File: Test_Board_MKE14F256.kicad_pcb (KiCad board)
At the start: 4 copper layers, 115 parts, among them P1 CONN_01X02, P10 CONN_01X01, P11 CONN_01X01, P12 CONN_01X01, P13 CONN_01X01, P14 CONN_01X01, P15 CONN_01X01, P16 CONN_01X01, P17 CONN_01X01, P18 CONN_01X01, P19 CONN_01X01, P2 CONN_01X04, P20 CONN_01X01, P21 CONN_01X01, P22 CONN_01X01, P23 CONN_01X01, P24 CONN_01X01, P25 CONN_01X01, P26 CONN_01X01, P27 CONN_01X01, P28 CONN_01X04, P5 CONN_01X05, P6 CONN_01X04, P7 CONN_01X01, P8 CONN_01X01, P9 CONN_01X01, U1 TS30042, U2 NCP700B, U3 MIC2288, U4 ADS79XX, U5 REF3030, U6 TSV524A, U7 MKE14F256_v.1.2, Y1 ABMM2-8.000MHZ-E2-T

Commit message: changed usd slot
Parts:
- XS1: footprint .pretty:uSDcard -> .pretty:HIROSE-MICROSD-DM3AT-SF
- moved R27 153.8 mm to (26.7, 31.0)
- moved R26 150.1 mm to (26.7, 38.7)
- moved D7 149.3 mm to (33.3, 31.6)
- moved D8 144.1 mm to (34.4, 40.1)
- moved R25 143.0 mm to (268.8, 17.0)
- moved C29 139.2 mm to (266.2, 19.3)
- moved C33 138.5 mm to (42.5, 35.3)
- moved C35 134.8 mm to (43.6, 40.5)
- moved XS1 126.4 mm to (267.4, 38.5)
- moved R22 117.0 mm to (265.9, 157.4)
- moved R21 116.2 mm to (266.8, 153.0)
- moved R20 115.2 mm to (267.9, 147.4)
- moved R19 113.9 mm to (268.3, 142.0)
- moved D6 112.5 mm to (261.2, 156.7)
- moved P28 110.9 mm to (29.8, 101.9)
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
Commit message: All parts in places (exept :Leds)
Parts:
- moved R27 160.3 mm to (181.8, 71.3)
- moved R26 159.2 mm to (181.8, 74.8)
- moved P6 158.0 mm to (188.2, 67.0), turned to 270 degrees
- moved P2 151.0 mm to (188.2, 61.8), turned to 90 degrees
- moved D7 148.5 mm to (176.4, 71.3), turned to 180 degrees
- moved D8 146.2 mm to (176.4, 74.8), turned to 180 degrees
- moved C33 142.1 mm to (179.0, 74.8), turned to 270 degrees
- moved C35 138.8 mm to (179.0, 71.3), turned to 270 degrees
- moved P28 118.4 mm to (146.3, 80.6), turned to 90 degrees
- moved C1 115.9 mm to (158.3, 92.1)
- moved C38 115.9 mm to (159.2, 89.8)
- moved L1 115.9 mm to (164.3, 83.0)
- moved C3 115.9 mm to (161.3, 83.1)
- moved U1 115.9 mm to (163.3, 88.5)
- moved C4 115.9 mm to (158.9, 83.1)
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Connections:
- P2 pad 1: V_in_4 -> V_in_3
- P2 pad 3: V_in_3 -> V_in_2
- P2 pad 5: V_in_2 -> V_in_4
- R31 pad 2: Net-(R31-Pad2) -> OpAmp_Out2
- R32 pad 2: Net-(R32-Pad2) -> OpAmp_Out4
- R5 pad 1: ADC_2 -> OpAmp_Out2
- R6 pad 1: ADC_1 -> OpAmp_Out4
- U6 pad 13: Net-(R32-Pad2) -> OpAmp_Out4
- U6 pad 14: Net-(R32-Pad2) -> OpAmp_Out4
- U6 pad 8: Net-(R31-Pad2) -> OpAmp_Out2
- U6 pad 9: Net-(R31-Pad2) -> OpAmp_Out2
- U7 pad 51: ADC_1 -> ADC_3
- U7 pad 52: ADC_2 -> ADC_1
- U7 pad 53: ADC_3 -> ADC_4
- U7 pad 54: ADC_4 -> ADC_2
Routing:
- net V_in_4: track 0.00 -> 34.5 mm
- net V_in_2: track 0.00 -> 30.6 mm
- net ADC_3: track 0.00 -> 16.5 mm
- net ADC_2: track 0.00 -> 15.1 mm
- net V_in_3: track 0.00 -> 14.9 mm
- net +3V3: track 0.00 -> 7.65 mm, vias 0 -> 2
- net ADC_1: track 0.00 -> 7.49 mm
- net ADC_4: track 0.00 -> 5.40 mm
- net GND: track 0.00 -> 5.06 mm
- net Net-(C23-Pad1): track 0.00 -> 4.65 mm
- net Net-(C19-Pad1): track 0.00 -> 4.60 mm
- net Net-(C18-Pad1): track 0.00 -> 4.55 mm
- net Net-(C24-Pad1): track 0.00 -> 4.53 mm
- net Net-(R30-Pad2): track 0.00 -> 2.60 mm
- net OpAmp_Out2: track 0.00 -> 2.58 mm
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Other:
- net class Default: via_dia 0.6 -> 0.65; via_drill 0.4 -> 0.3

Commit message: Started with tracking
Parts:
- moved P22 61.3 mm to (65.1, 118.8)
- moved P23 61.3 mm to (65.1, 118.8)
- moved P24 61.3 mm to (65.1, 118.8)
- moved P25 61.3 mm to (65.1, 118.8)
- moved P26 61.3 mm to (65.1, 118.8)
- moved P27 61.3 mm to (65.1, 118.8)
- moved LS 35.4 mm to (93.8, 124.8)
- moved HS 32.5 mm to (94.3, 117.7)
- moved DC_Vin 23.7 mm to (102.1, 109.9)
- moved GND 22.6 mm to (112.9, 128.2)
- moved ADC_4 20.1 mm to (145.8, 109.7)
- moved GND 18.9 mm to (112.7, 123.2)
- moved ADC_3 18.7 mm to (143.2, 116.1)
- moved Vref 18.5 mm to (134.4, 125.8)
- moved GND 17.2 mm to (122.4, 126.3)
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- renumbered P11 to +3.3V, P16 to +3.3V, P7 to ADC_1, P8 to ADC_2, P9 to ADC_3, P10 to ADC_4, P17 to DC_3V6, P18 to DC_Vin, P12 to GND, P13 to GND, P14 to GND, P15 to GND, P20 to HS, P21 to LS, P19 to Vref
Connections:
- Y1 pad 2: Net-(C28-Pad1) -> (no net)
- Y1 pad 3: (no net) -> Net-(C28-Pad1)
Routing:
- net GND: track 5.06 -> 47.3 mm, vias 0 -> 14
- net +3V3: track 7.65 -> 45.0 mm, vias 2 -> 8
- net uSD_SPI0_CS0: track 0.00 -> 16.6 mm
- net uSD_SPI0_DI: track 0.00 -> 15.3 mm
- net uSD_SPI0_SCLK: track 0.00 -> 15.2 mm
- net UART1_RX: track 0.00 -> 14.0 mm
- net uSD_SPI0_DO: track 0.00 -> 13.7 mm
- net Net-(C28-Pad1): track 0.00 -> 11.6 mm
- net UART1_TX: track 0.00 -> 11.3 mm
- net Net-(C27-Pad1): track 0.00 -> 11.1 mm
- net Net-(P6-Pad2): track 0.00 -> 5.16 mm
- net Net-(P6-Pad3): track 0.00 -> 4.71 mm
- net (no net): track 0.00 -> 4.46 mm, vias 0 -> 1
- net Vref: track 0.00 -> 3.43 mm
- net ADC_3: track 16.5 -> 19.4 mm
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
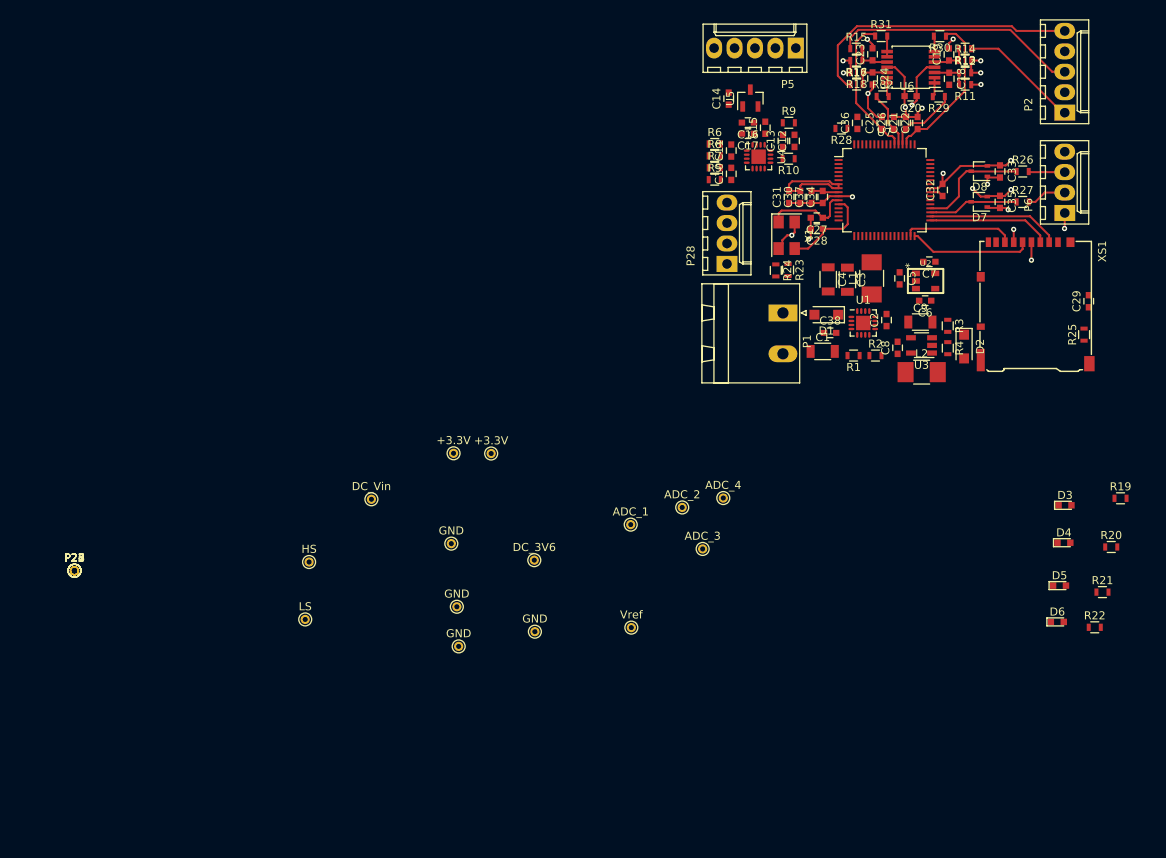
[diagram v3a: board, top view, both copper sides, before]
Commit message: added missing parts (SPI conn / Boost Conn/ drills..)
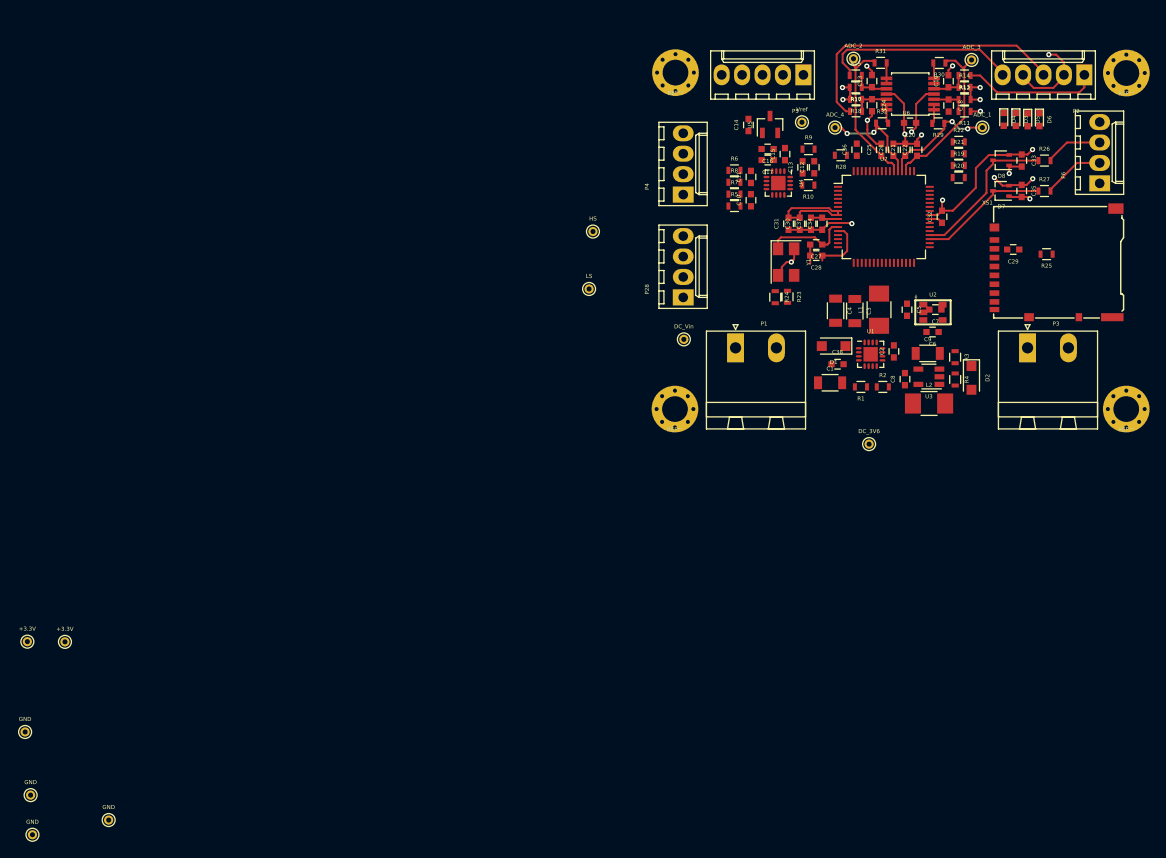
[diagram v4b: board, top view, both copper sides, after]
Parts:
- removed P22, P23, P24, P25, P26, P27: CONN_01X01, Connect:PINTST
- added P3: CONN_01X02, Connectors_Phoenix:PhoenixContact_MSTBA-G_02x5.08mm_Angled, F.Cu at (183.6, 91.1)
- added P4: CONN_01X04, Connectors_Molex:Molex_KK-6410-04_04x2.54mm_Straight, F.Cu at (140.8, 72.0)
- added REF**: 3mm_holes, .pretty:3mm_holes, F.Cu at (139.8, 98.7)
- added REF**: 3mm_holes, .pretty:3mm_holes, F.Cu at (139.9, 56.8)
- added REF**: 3mm_holes, .pretty:3mm_holes, F.Cu at (195.9, 98.7)
- added REF**: 3mm_holes, .pretty:3mm_holes, F.Cu at (195.9, 56.9)
- moved ADC_3 69.4 mm to (176.7, 55.3)
- moved Vref 66.3 mm to (155.6, 63.0)
- moved ADC_1 65.9 mm to (178.0, 63.7)
- moved R22 62.7 mm to (175.1, 65.5)
- moved D6 62.5 mm to (185.1, 62.7), turned to 270 degrees
- moved ADC_2 59.7 mm to (162.0, 55.1)
- moved D5 58.0 mm to (183.6, 62.7), turned to 270 degrees
- moved GND 57.9 mm to (59.7, 146.7)
- moved GND 57.9 mm to (59.9, 151.6)
- moved +3.3V 57.9 mm to (59.3, 127.6)
- moved GND 57.9 mm to (59.0, 138.8)
- moved GND 57.9 mm to (69.4, 149.8)
- moved +3.3V 57.9 mm to (64.0, 127.6)
- moved R21 57.3 mm to (175.1, 66.9)
- moved HS 54.2 mm to (129.6, 76.6)
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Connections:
- P2 pad 3: V_in_2 -> V_in_4
- P2 pad 5: V_in_4 -> V_in_2
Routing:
- net uSD_SPI0_CS0: track 16.6 -> 0.29 mm
- net uSD_SPI0_DI: track 15.3 -> 0.00 mm
- net uSD_SPI0_SCLK: track 15.2 -> 0.00 mm
- net uSD_SPI0_DO: track 13.7 -> 0.00 mm
- net GND: track 47.3 -> 55.9 mm, vias 14 -> 13
- net ADC_4: track 7.08 -> 13.5 mm, vias 0 -> 2
- net V_in_2: track 30.6 -> 24.6 mm
- net UART1_RX: track 14.0 -> 19.3 mm
- net ADC_1: track 9.03 -> 14.3 mm, vias 0 -> 2
- net UART1_TX: track 11.3 -> 16.3 mm
- net Net-(C28-Pad1): track 11.6 -> 7.35 mm
- net Net-(P6-Pad3): track 4.71 -> 7.39 mm
- net Net-(P6-Pad2): track 5.16 -> 7.68 mm
- net +3V3: track 45.0 -> 46.9 mm, vias 8 -> 6
- net V_in_3: track 14.9 -> 16.8 mm
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
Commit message: still the regulators & Planes fill
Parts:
- added P10, P11, P12, P13, P14, P15, P16, P17, P18, P19, P20, P21, P22, P23, P24, P25, P26, P27, P7, P8, P9: CONN_01X01, Connect:PINTST, F.Cu at (168.1, 112.3)
- moved +3.3V 41.2 mm to (93.4, 104.4)
- moved GND 41.2 mm to (103.5, 126.5)
- moved GND 41.2 mm to (93.1, 115.6)
- moved +3.3V 41.2 mm to (98.0, 104.4)
- moved GND 41.2 mm to (93.8, 123.4)
- moved GND 41.2 mm to (94.0, 128.4)
- moved Vref 16.5 mm to (147.8, 77.7)
- moved C14 12.4 mm to (150.5, 75.7)
- moved U5 12.2 mm to (153.1, 75.5)
- moved R25 9.80 mm to (176.2, 79.9), turned to 90 degrees
- moved C4 5.60 mm to (165.3, 85.7), turned to 180 degrees
- moved C29 5.29 mm to (177.7, 82.1), turned to 90 degrees
- moved R22 5.15 mm to (174.9, 70.6)
- moved L1 4.56 mm to (165.2, 90.9), turned to 0 degrees
- moved C31 4.40 mm to (156.9, 72.4), turned to 0 degrees
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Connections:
- U1 pad 16: Net-(U1-Pad16) -> Net-(C2-Pad2)
- U7 pad 25: led_red -> Net-(U7-Pad25)
- U7 pad 26: led_yel -> ADC_PDEN
- U7 pad 27: led_grn -> Net-(U7-Pad27)
- U7 pad 28: led_blu -> Net-(U7-Pad28)
- U7 pad 43: ADC_PDEN -> Net-(U7-Pad43)
- U7 pad 47: Net-(U7-Pad47) -> led_blu
- U7 pad 48: Net-(U7-Pad48) -> led_red
- U7 pad 49: Net-(U7-Pad49) -> led_grn
- U7 pad 50: Net-(U7-Pad50) -> led_yel
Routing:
- net GND: track 55.9 -> 122.1 mm, vias 13 -> 28
- net ADC_SPI1_MOSI_ADC_CH_SEL: track 0.00 -> 51.0 mm, vias 0 -> 2
- net ADC_SPI1_CS0: track 0.00 -> 45.6 mm, vias 0 -> 2
- net OpAmp_Out2: track 2.58 -> 39.3 mm, vias 0 -> 2
- net ADC_SPI1_SCLK: track 0.00 -> 31.6 mm, vias 0 -> 1
- net Vref: track 3.43 -> 33.6 mm, vias 0 -> 4
- net ADC_SPI1_SDO: track 0.00 -> 28.3 mm, vias 0 -> 1
- net OpAmp_Out4: track 2.41 -> 27.3 mm, vias 0 -> 2
- net SWD_RESET: track 0.00 -> 21.0 mm
- net ADC_PDEN: track 0.00 -> 19.1 mm, vias 0 -> 2
- net SWD_DIO_TGTMCU: track 0.00 -> 18.5 mm, vias 0 -> 1
- net SWD_CLK: track 0.00 -> 17.0 mm, vias 0 -> 2
- net Net-(D6-Pad2): track 0.00 -> 16.2 mm
- net Net-(C12-Pad1): track 0.00 -> 15.9 mm
- net DC_Vin: track 0.00 -> 14.8 mm
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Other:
- board outline added: 62.8 x 49.7 mm

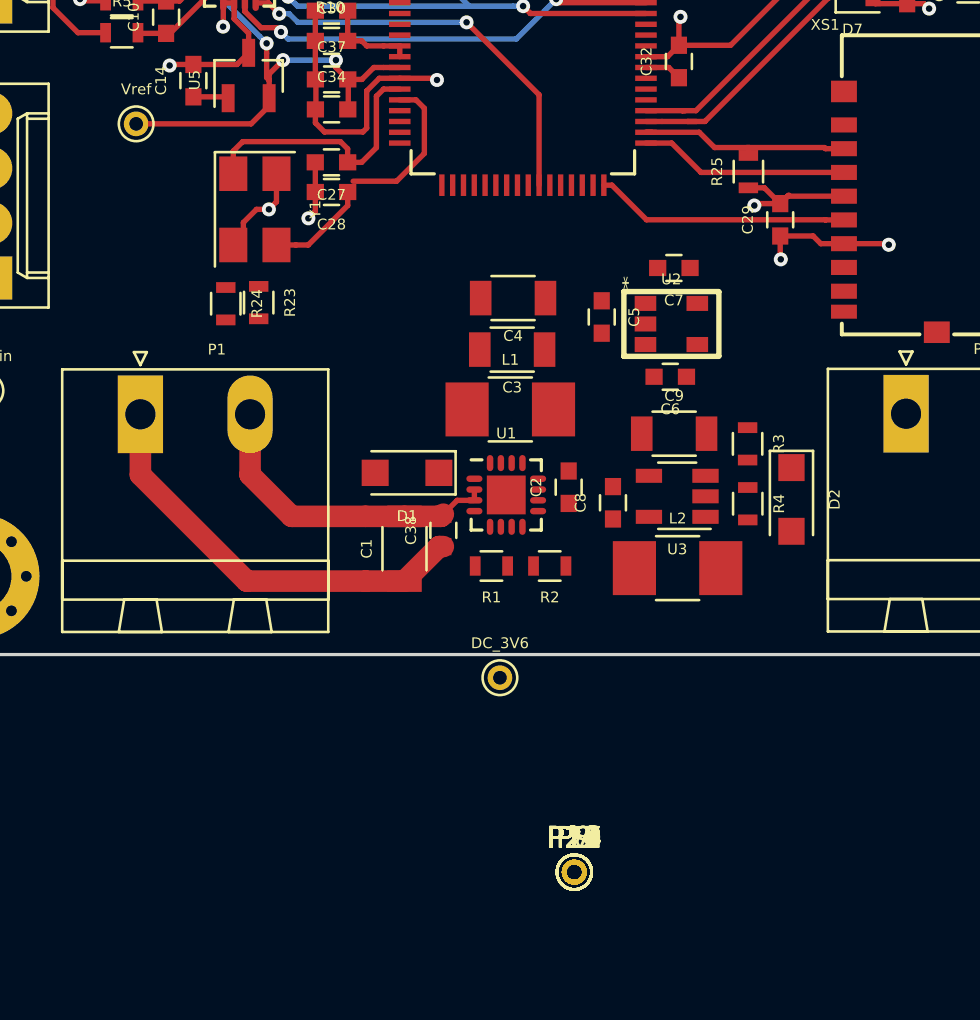
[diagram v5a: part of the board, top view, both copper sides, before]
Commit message: routed the Buck & LDO ==> Still Boost
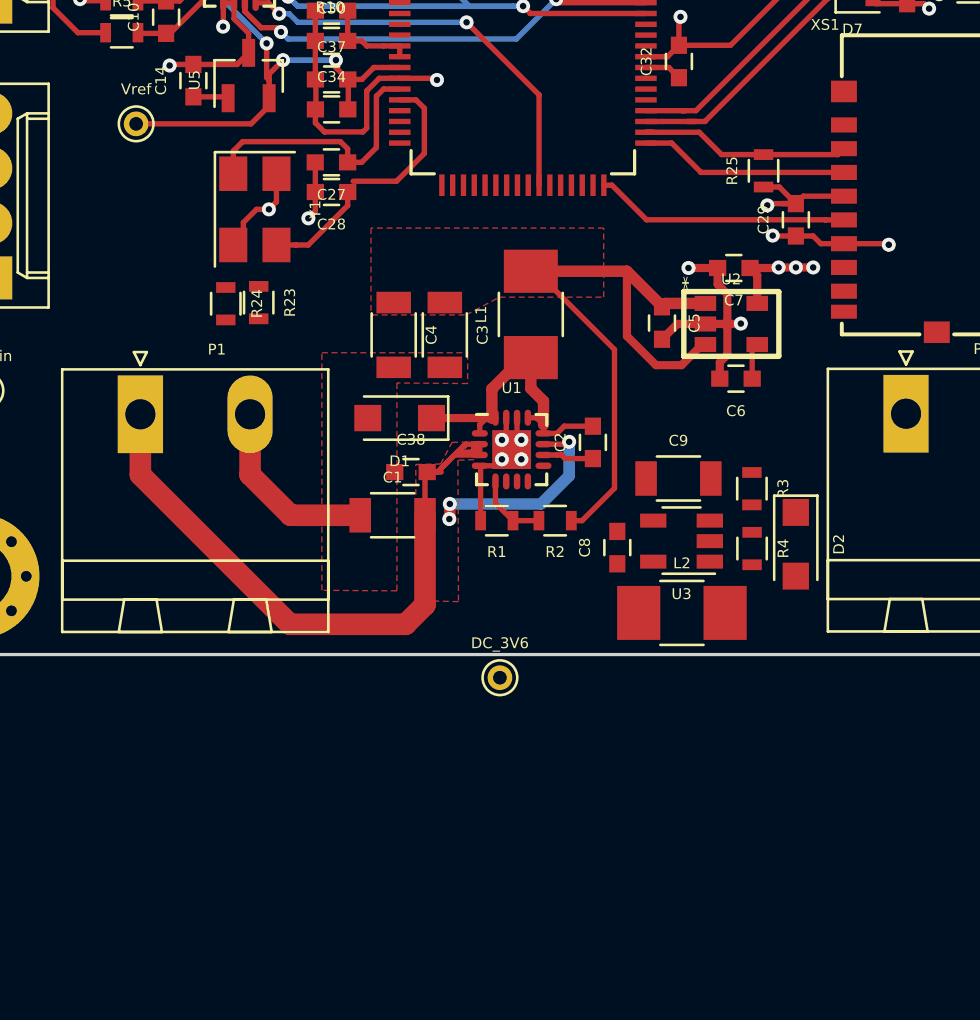
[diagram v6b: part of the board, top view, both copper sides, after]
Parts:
- removed P10, P11, P12, P13, P14, P15, P16, P17, P18, P19, P20, P21, P22, P23, P24, P25, P26, P27, P7, P8, P9: CONN_01X01, Connect:PINTST
- moved C4 5.79 mm to (159.8, 87.4), turned to 270 degrees
- moved L1 4.50 mm to (166.1, 86.5), turned to 90 degrees
- moved C3 3.19 mm to (162.1, 87.4), turned to 270 degrees
- moved C38 3.09 mm to (160.6, 93.8), turned to 0 degrees
- moved C6 3.04 mm to (175.6, 89.5)
- moved C5 2.81 mm to (172.2, 86.9)
- moved C7 2.78 mm to (175.5, 84.3)
- moved U2 2.78 mm to (175.4, 86.9)
- moved D1 2.56 mm to (160.1, 91.3)
- moved C2 2.36 mm to (169.0, 92.4)
- moved R1 2.11 mm to (164.6, 96.0)
- moved R2 2.11 mm to (167.2, 96.0)
- moved U1 2.11 mm to (165.2, 92.7)
- moved D2 2.08 mm to (178.4, 97.1)
- moved C8 2.08 mm to (170.1, 97.3)
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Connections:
- P1 pad 1: GND -> DC_Vin
- P1 pad 2: DC_Vin -> GND
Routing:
- net DC_3V6: track 0.00 -> 30.9 mm
- net DC_Vin: track 14.8 -> 43.1 mm, vias 0 -> 3
- net Net-(C2-Pad2): track 0.00 -> 15.2 mm
- net GND: track 122.1 -> 130.2 mm, vias 28 -> 34
- net +3V3: track 46.9 -> 51.2 mm, vias 9 -> 12
- net Net-(R1-Pad1): track 0.00 -> 3.35 mm
- net Net-(C2-Pad1): track 0.00 -> 2.36 mm
- net Net-(C6-Pad1): track 0.00 -> 1.68 mm
- added copper zone on F.Cu, net DC_3V6
- added copper zone on F.Cu, net DC_Vin
- added copper zone on F.Cu, net GND

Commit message: connected Boost. Still inner layers
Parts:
- R3: value 43k -> 91k
- R4: value 3.9k -> 8.2k
- moved GND 107.1 mm to (196.0, 91.5)
- moved GND 96.7 mm to (169.0, 55.5)
- moved +3.3V 84.8 mm to (178.2, 76.7)
- moved GND 81.7 mm to (140.8, 61.4)
- moved +3.3V 71.8 mm to (165.0, 99.8)
- moved GND 66.7 mm to (153.2, 86.6)
- moved LS 19.5 mm to (148.6, 84.0)
- moved HS 19.4 mm to (148.6, 80.6)
- moved R24 10.1 mm to (145.4, 78.3)
- moved R23 8.45 mm to (145.4, 83.6), turned to 90 degrees
- moved C8 7.10 mm to (174.8, 91.9), turned to 0 degrees
- moved L2 5.55 mm to (171.8, 94.9), turned to 270 degrees
- moved C9 5.09 mm to (178.0, 94.8), turned to 270 degrees
- moved DC_3V6 4.86 mm to (168.0, 99.8)
- moved D2 4.29 mm to (175.1, 99.9), turned to 180 degrees
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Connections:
- P28 pad 1: PWM_HS -> PWM_LS
- P28 pad 4: PWM_LS -> PWM_HS
- P3 pad 1: +15V -> GND
- P3 pad 2: GND -> +15V
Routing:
- net Boost_Enable: track 0.00 -> 30.8 mm, vias 0 -> 2
- net PWM_LS: track 0.00 -> 25.5 mm, vias 0 -> 1
- net PWM_HS: track 0.00 -> 25.4 mm, vias 0 -> 1
- net GND: track 130.2 -> 149.2 mm, vias 34 -> 35
- net DC_Vin: track 43.1 -> 25.2 mm
- net +15V: track 0.00 -> 17.9 mm
- net uSD_SPI0_DO: track 0.00 -> 13.6 mm
- net Net-(D2-Pad2): track 0.00 -> 10.4 mm
- net Net-(R3-Pad2): track 0.00 -> 3.00 mm
- net +3V3: track 51.2 -> 53.9 mm, vias 12 -> 13
- net DC_3V6: track 30.9 -> 33.1 mm
- net Vref: track 33.6 -> 34.9 mm
- added copper zone on F.Cu, net +15V
